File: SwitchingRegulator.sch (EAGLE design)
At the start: 31 parts, among them J1 APP_2POS_CONFIG5V_HORIZ, J2 APP_2POS_CONFIG5V_HORIZ, J3 APP_2POS_CONFIG5V_HORIZ, Q1 Q_OKI-78SR, Q2 Q_CSD18532KCSPCB

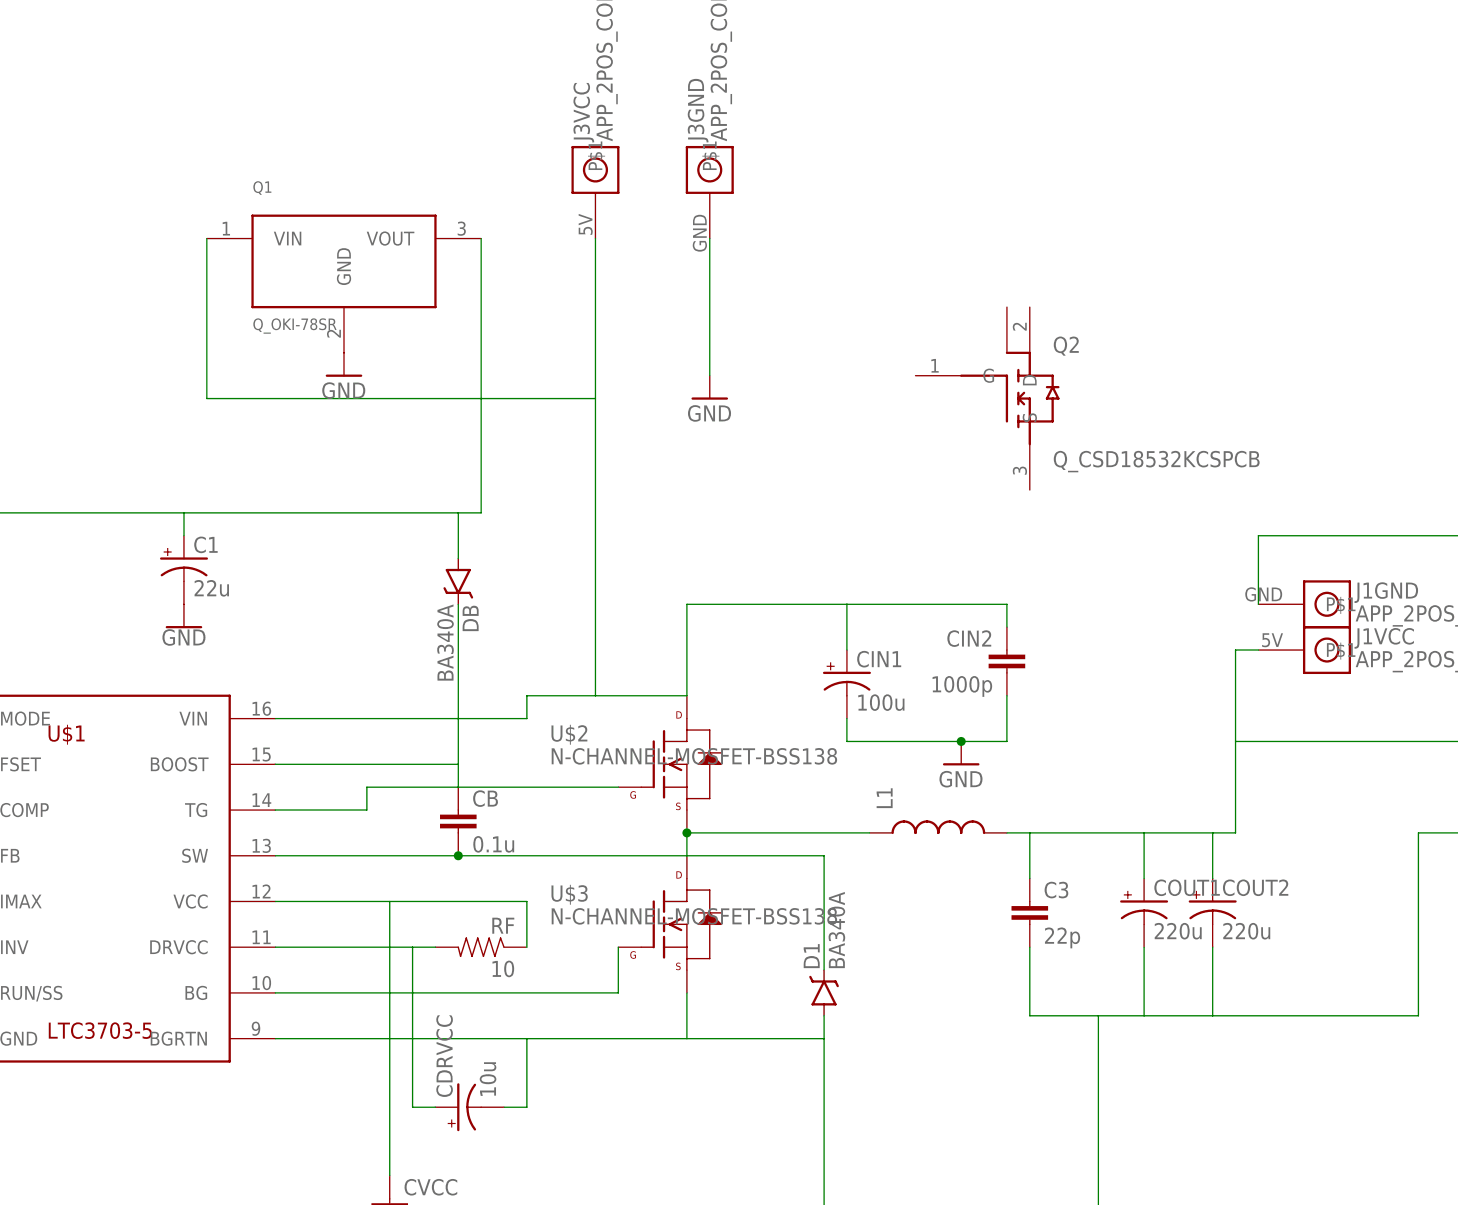
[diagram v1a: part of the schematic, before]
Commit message: Updated with all real components
Added devices for inductor, diodes, and mosfets
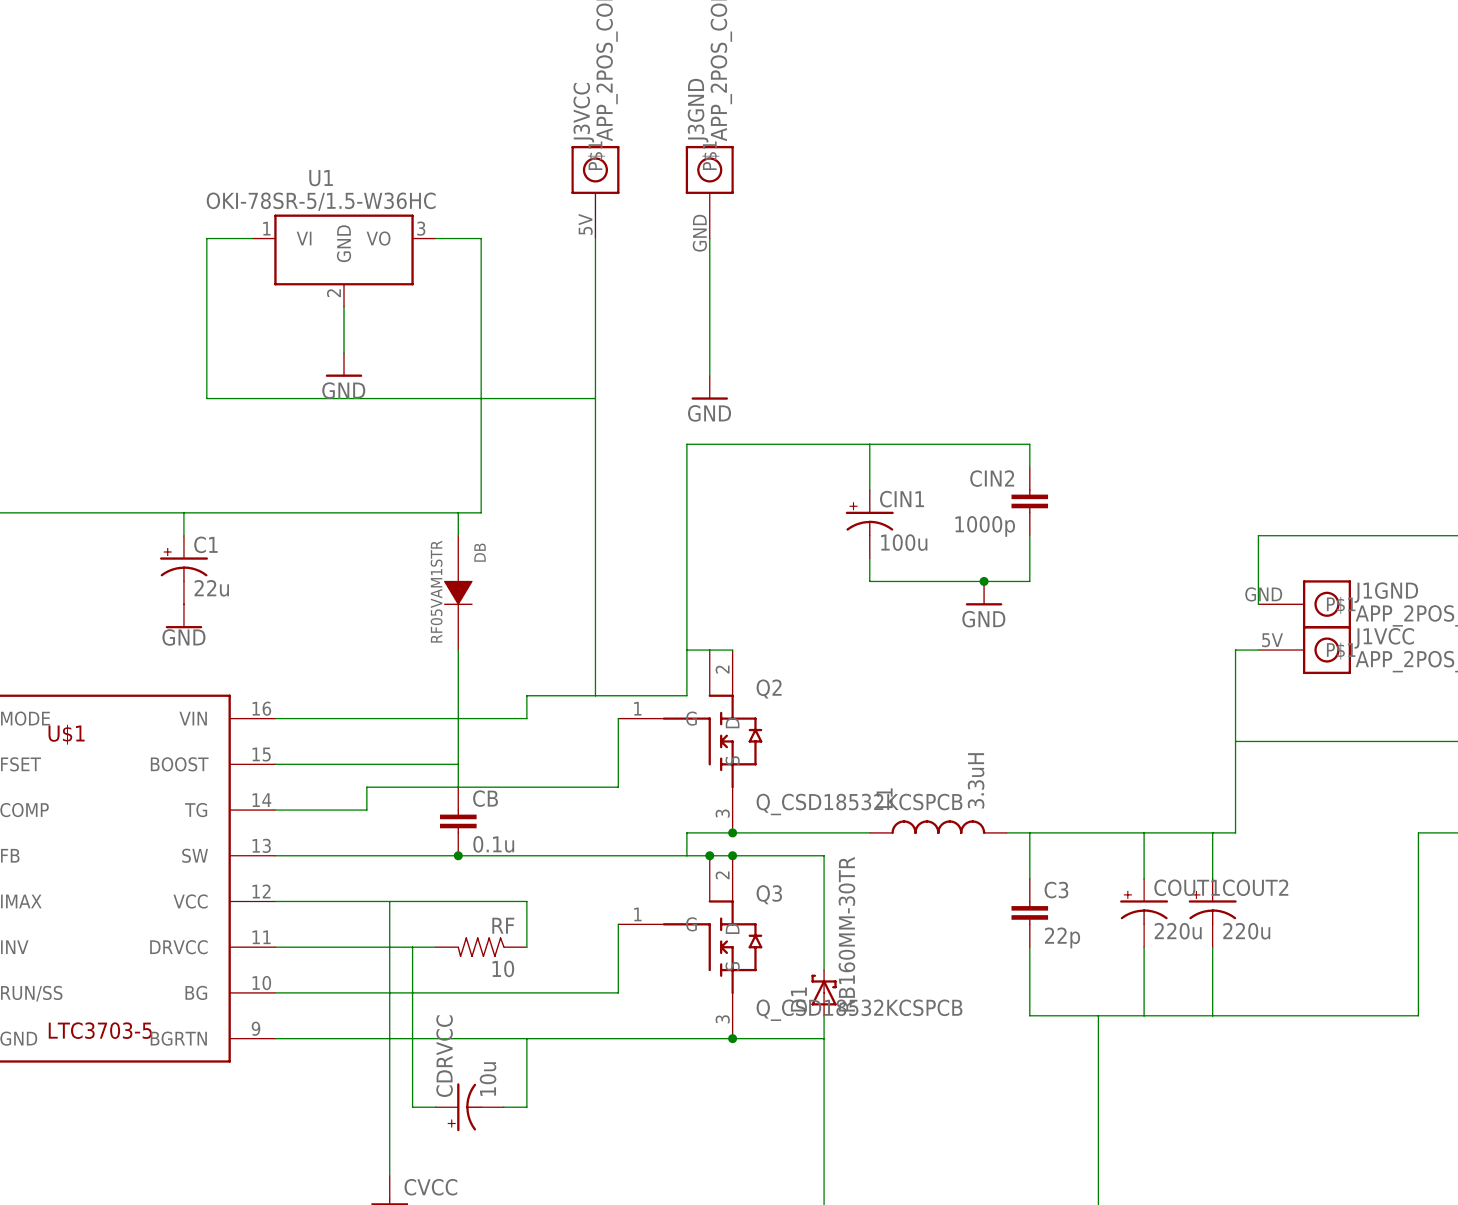
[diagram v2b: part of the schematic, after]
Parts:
- removed Q1: Q_OKI-78SR, MRDT-2014-All:Q_OKI-78SR
- removed U$2, U$3: N-CHANNEL-MOSFET-BSS138, GeekAmmo:N-CHANNEL-MOSFET-BSS138
- added Q3: Q_CSD18532KCSPCB, MRDT-2014-All:Q_CSD18532KCSPCB
- added U1: OKI-78SR-5/1.5-W36HC, MRDT-ICs:OKI-78SR-5/1.5-W36HC
- CIN1: device MRDT-2015-PowerBoard:B41858C9107M000 -> buckconverter:B41858C9107M000
- COUT1, COUT2: device MRDT-2015-PowerBoard:EGPD101ELL221MK25H -> buckconverter:EGPD101ELL221MK25H
- D1: value BA340A -> RB160MM-30TR; device SparkFun-DiscreteSemi:B340A -> buckconverter:RB160MM-30TR
- DB: value BA340A -> RF05VAM1STR; device SparkFun-DiscreteSemi:B340A -> buckconverter:RF05VAM1STR
- L1: value (none) -> 3.3uH; device SparkFun-Passives:INDUCTOR0805 -> buckconverter:PQ3218-3R3-70-T
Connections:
- net GND: now also Q3.S, U1.GND; no longer Q1.GND, U$3.S
- net N$1: now also DB.K; no longer DB.C
- net N$16: now also Q3.G; no longer U$3.G
- net N$17: now also Q2.S, Q3.D, Q3.P$1; no longer U$2.S, U$3.D
- net N$2: now also Q2.G; no longer U$2.G
- net N$5: now also U1.VO; no longer Q1.VOUT
- net VBATT: now also Q2.D, Q2.P$1, U1.VI; no longer Q1.VIN, U$2.D
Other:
- moved on the sheet: CIN1, CIN2, Q2

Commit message: Board design initiated
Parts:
- CDRVCC: device SparkFun-Passives:CAP_POL1206 -> SparkFun-Passives:CAP0603-CAP
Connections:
- net GND: now also CDRVCC.2; no longer CDRVCC.-
- net N$15: now also CDRVCC.1; no longer CDRVCC.+
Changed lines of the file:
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@@
 <?xml version="1.0" encoding="utf-8"?>
 <!DOCTYPE eagle SYSTEM "eagle.dtd">
-<eagle version="7.4.0">
+<eagle version="8.3.2">
 <drawing>
 <settings>
 <setting alwaysvectorfont="no"/>
+<setting keepoldvectorfont="yes"/>
 <setting verticaltext="up"/>
 </settings>
@@
 <part name="GND1" library="SparkFun-Aesthetics" deviceset="GND" device=""/>
 <part name="GND3" library="SparkFun-Aesthetics" deviceset="GND" device=""/>
-<part name="CDRVCC" library="SparkFun-Passives" deviceset="CAP_POL" device="1206" value="10u"/>
 <part name="GND4" library="SparkFun-Aesthetics" deviceset="GND" device=""/>
 <part name="GND5" library="SparkFun-Aesthetics" deviceset="GND" device=""/>
@@
 <part name="DB" library="buckconverter" deviceset="RF05VAM1STR" device=""/>
 <part name="U1" library="MRDT-ICs" deviceset="OKI-78SR-*/1.5-W36?C" device="H" technology="5"/>
+<part name="CDRVCC" library="SparkFun-Passives" deviceset="CAP" device="0603-CAP" value="10u"/>
 </parts>
 <sheets>
@@
 <instance part="GND1" gate="1" x="30.48" y="73.66"/>
 <instance part="GND3" gate="1" x="182.88" y="147.32"/>
-<instance part="CDRVCC" gate="G$1" x="124.46" y="91.44" rot="R90"/>
 <instance part="GND4" gate="1" x="152.4" y="170.18"/>
 <instance part="GND5" gate="1" x="111.76" y="172.72"/>
@@
 <instance part="DB" gate="G$1" x="124.46" y="147.32" rot="R270"/>
 <instance part="U1" gate="G$1" x="109.22" y="187.96"/>
+<instance part="CDRVCC" gate="G$1" x="127" y="91.44" rot="R90"/>
 </instances>
 <busses>
@@
 <wire x1="195.58" y1="101.6" x2="195.58" y2="76.2" width="0.1524" layer="91"/>
 <wire x1="195.58" y1="76.2" x2="165.1" y2="76.2" width="0.1524" layer="91"/>
-<pinref part="CDRVCC" gate="G$1" pin="-"/>
 <wire x1="129.54" y1="91.44" x2="132.08" y2="91.44" width="0.1524" layer="91"/>
 <wire x1="132.08" y1="91.44" x2="132.08" y2="99.06" width="0.1524" layer="91"/>
@@
 <junction x="154.94" y="99.06"/>
 <pinref part="D1" gate="G$1" pin="A"/>
+<pinref part="CDRVCC" gate="G$1" pin="2"/>
 </segment>
 <segment>
@@
 <pinref part="U$1" gate="G$1" pin="DRVCC"/>
 <wire x1="121.92" y1="109.22" x2="119.38" y2="109.22" width="0.1524" layer="91"/>
-<pinref part="CDRVCC" gate="G$1" pin="+"/>
 <wire x1="119.38" y1="109.22" x2="104.14" y2="109.22" width="0.1524" layer="91"/>
 <wire x1="121.92" y1="91.44" x2="119.38" y2="91.44" width="0.1524" layer="91"/>
 <wire x1="119.38" y1="91.44" x2="119.38" y2="109.22" width="0.1524" layer="91"/>
-</segment>
-</net>
+<pinref part="CDRVCC" gate="G$1" pin="1"/>
+</segment>
+</net>

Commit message: Major rearrangements
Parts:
- D1: value RB160MM-30TR -> RBR3MM30ATR; device buckconverter:RB160MM-30TR -> buckconverter:RBR3MM30ATR
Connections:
- removed net N$12: CC3.2, R1.1
- removed net N$5: C1.+, DB.A, U$1.MODE, U1.VO
- net N$15: now also C1.+, DB.A, U$1.MODE, U1.VO
- net VOUT12+: now also CC3.2, R1.1
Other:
- moved on the sheet: CB
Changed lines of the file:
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@@
 <part name="CIN1" library="buckconverter" deviceset="B41858C9107M000" device="" value="100u"/>
 <part name="Q3" library="MRDT-2014-All" deviceset="Q_CSD18532KCS" device="PCB"/>
-<part name="D1" library="buckconverter" deviceset="RB160MM-30TR" device=""/>
+<part name="D1" library="buckconverter" deviceset="RBR3MM30ATR" device=""/>
 <part name="DB" library="buckconverter" deviceset="RF05VAM1STR" device=""/>
 <part name="U1" library="MRDT-ICs" deviceset="OKI-78SR-*/1.5-W36?C" device="H" technology="5"/>
@@
 </plain>
 <instances>
-<instance part="CB" gate="G$1" x="124.46" y="121.92"/>
+<instance part="CB" gate="G$1" x="144.78" y="121.92"/>
 <instance part="CVCC" gate="G$1" x="116.84" y="78.74"/>
 <instance part="CC3" gate="G$1" x="-30.48" y="76.2"/>
@@
 <wire x1="0" y1="109.22" x2="0" y2="116.84" width="0.1524" layer="91"/>
 <wire x1="12.7" y1="109.22" x2="0" y2="109.22" width="0.1524" layer="91"/>
+<junction x="0" y="109.22"/>
+<junction x="-10.16" y="96.52"/>
+<junction x="0" y="116.84"/>
+<junction x="38.1" y="116.84"/>
 </segment>
 </net>
@@
 <pinref part="D1" gate="G$1" pin="A"/>
 <pinref part="CDRVCC" gate="G$1" pin="2"/>
+<junction x="30.48" y="114.3"/>
+<junction x="30.48" y="104.14"/>
+<junction x="30.48" y="99.06"/>
+<junction x="45.72" y="99.06"/>
+<junction x="132.08" y="99.06"/>
+<junction x="165.1" y="76.2"/>
+<junction x="195.58" y="101.6"/>
+<junction x="200.66" y="101.6"/>
+<junction x="208.28" y="101.6"/>
+<junction x="243.84" y="137.16"/>
+<junction x="30.48" y="109.22"/>
+<junction x="116.84" y="76.2"/>
+<junction x="165.1" y="99.06"/>
 </segment>
 <segment>
@@
 </segment>
 </net>
-<net name="N$12" class="0">
-<segment>
-<pinref part="CC3" gate="G$1" pin="2"/>
-<wire x1="-30.48" y1="73.66" x2="-30.48" y2="66.04" width="0.1524" layer="91"/>
-<pinref part="R1" gate="G$1" pin="1"/>
-<wire x1="-30.48" y1="66.04" x2="-10.16" y2="66.04" width="0.1524" layer="91"/>
-<wire x1="-10.16" y1="66.04" x2="-10.16" y2="86.36" width="0.1524" layer="91"/>
-</segment>
-</net>
 <net name="N$13" class="0">
 <segment>
@@
 <wire x1="132.08" y1="109.22" x2="132.08" y2="114.3" width="0.1524" layer="91"/>
 <wire x1="132.08" y1="114.3" x2="116.84" y2="114.3" width="0.1524" layer="91"/>
+<junction x="116.84" y="114.3"/>
 </segment>
 </net>
@@
 <wire x1="119.38" y1="91.44" x2="119.38" y2="109.22" width="0.1524" layer="91"/>
 <pinref part="CDRVCC" gate="G$1" pin="1"/>
+<pinref part="U$1" gate="G$1" pin="MODE"/>
+<wire x1="66.04" y1="134.62" x2="58.42" y2="134.62" width="0.1524" layer="91"/>
+<wire x1="58.42" y1="134.62" x2="58.42" y2="157.48" width="0.1524" layer="91"/>
+<wire x1="58.42" y1="157.48" x2="93.98" y2="157.48" width="0.1524" layer="91"/>
+<wire x1="93.98" y1="157.48" x2="119.38" y2="157.48" width="0.1524" layer="91"/>
+<wire x1="119.38" y1="157.48" x2="124.46" y2="157.48" width="0.1524" layer="91"/>
+<wire x1="124.46" y1="157.48" x2="127" y2="157.48" width="0.1524" layer="91"/>
+<wire x1="127" y1="187.96" x2="127" y2="157.48" width="0.1524" layer="91"/>
+<pinref part="C1" gate="G$1" pin="+"/>
+<wire x1="93.98" y1="157.48" x2="93.98" y2="154.94" width="0.1524" layer="91"/>
+<pinref part="DB" gate="G$1" pin="A"/>
+<wire x1="124.46" y1="154.94" x2="124.46" y2="157.48" width="0.1524" layer="91"/>
+<pinref part="U1" gate="G$1" pin="VO"/>
+<wire x1="121.92" y1="187.96" x2="127" y2="187.96" width="0.1524" layer="91"/>
+<wire x1="119.38" y1="109.22" x2="119.38" y2="157.48" width="0.1524" layer="91"/>
+<junction x="119.38" y="109.22"/>
+<junction x="124.46" y="157.48"/>
+<junction x="119.38" y="157.48"/>
+<junction x="93.98" y="157.48"/>
 </segment>
 </net>
@@
 <segment>
 <pinref part="U$1" gate="G$1" pin="SW"/>
-<wire x1="149.86" y1="119.38" x2="124.46" y2="119.38" width="0.1524" layer="91"/>
-<wire x1="124.46" y1="119.38" x2="104.14" y2="119.38" width="0.1524" layer="91"/>
+<wire x1="149.86" y1="119.38" x2="144.78" y2="119.38" width="0.1524" layer="91"/>
+<wire x1="144.78" y1="119.38" x2="104.14" y2="119.38" width="0.1524" layer="91"/>
 <wire x1="165.1" y1="106.68" x2="165.1" y2="119.38" width="0.1524" layer="91"/>
 <wire x1="165.1" y1="119.38" x2="154.94" y2="119.38" width="0.1524" layer="91"/>
@@
 <wire x1="149.86" y1="121.92" x2="149.86" y2="119.38" width="0.1524" layer="91"/>
 <pinref part="CB" gate="G$1" pin="2"/>
-<junction x="124.46" y="119.38"/>
+<junction x="144.78" y="119.38"/>
 <pinref part="L1" gate="G$1" pin="1"/>
 <pinref part="Q2" gate="G$1" pin="S"/>
@@
 <junction x="152.4" y="119.38"/>
 <pinref part="D1" gate="G$1" pin="C"/>
+<junction x="149.86" y="119.38"/>
 </segment>
 </net>
@@
 <segment>
 <pinref part="U$1" gate="G$1" pin="BOOST"/>
-<pinref part="CB" gate="G$1" pin="1"/>
 <wire x1="104.14" y1="129.54" x2="124.46" y2="129.54" width="0.1524" layer="91"/>
-<wire x1="124.46" y1="129.54" x2="124.46" y2="127" width="0.1524" layer="91"/>
 <pinref part="DB" gate="G$1" pin="K"/>
 <wire x1="124.46" y1="142.24" x2="124.46" y2="129.54" width="0.1524" layer="91"/>
+<pinref part="CB" gate="G$1" pin="1"/>
+<wire x1="124.46" y1="129.54" x2="144.78" y2="129.54" width="0.1524" layer="91"/>
+<wire x1="144.78" y1="129.54" x2="144.78" y2="127" width="0.1524" layer="91"/>
+<junction x="124.46" y="129.54"/>
 </segment>
 </net>
@@
 <pinref part="Q2" gate="G$1" pin="G"/>
 <wire x1="142.24" y1="134.62" x2="142.24" y2="127" width="0.1524" layer="91"/>
-</segment>
-</net>
-<net name="N$5" class="0">
-<segment>
-<pinref part="U$1" gate="G$1" pin="MODE"/>
-<wire x1="66.04" y1="134.62" x2="58.42" y2="134.62" width="0.1524" layer="91"/>
-<wire x1="58.42" y1="134.62" x2="58.42" y2="157.48" width="0.1524" layer="91"/>
-<wire x1="58.42" y1="157.48" x2="93.98" y2="157.48" width="0.1524" layer="91"/>
-<wire x1="93.98" y1="157.48" x2="124.46" y2="157.48" width="0.1524" layer="91"/>
-<wire x1="124.46" y1="157.48" x2="127" y2="157.48" width="0.1524" layer="91"/>
-<wire x1="127" y1="187.96" x2="127" y2="157.48" width="0.1524" layer="91"/>
-<pinref part="C1" gate="G$1" pin="+"/>
-<wire x1="93.98" y1="157.48" x2="93.98" y2="154.94" width="0.1524" layer="91"/>
-<pinref part="DB" gate="G$1" pin="A"/>
-<wire x1="124.46" y1="154.94" x2="124.46" y2="157.48" width="0.1524" layer="91"/>
-<pinref part="U1" gate="G$1" pin="VO"/>
-<wire x1="121.92" y1="187.96" x2="127" y2="187.96" width="0.1524" layer="91"/>
 </segment>
 </net>
@@
 <pinref part="U1" gate="G$1" pin="VI"/>
 <wire x1="101.6" y1="187.96" x2="96.52" y2="187.96" width="0.1524" layer="91"/>
+<junction x="139.7" y="137.16"/>
+<junction x="149.86" y="142.24"/>
+<junction x="152.4" y="142.24"/>
+<junction x="170.18" y="165.1"/>
+<junction x="139.7" y="170.18"/>
 </segment>
 </net>
@@
 <pinref part="COUT1" gate="G$1" pin="+"/>
 <pinref part="COUT2" gate="G$1" pin="+"/>
-</segment>
-</net>
+<pinref part="CC3" gate="G$1" pin="2"/>
+<wire x1="-30.48" y1="73.66" x2="-30.48" y2="66.04" width="0.1524" layer="91"/>
+<pinref part="R1" gate="G$1" pin="1"/>
+<wire x1="-30.48" y1="66.04" x2="-10.16" y2="66.04" width="0.1524" layer="91"/>
+<wire x1="-10.16" y1="66.04" x2="-10.16" y2="68.58" width="0.1524" layer="91"/>
+<wire x1="-10.16" y1="68.58" x2="-10.16" y2="86.36" width="0.1524" layer="91"/>
+<wire x1="-10.16" y1="68.58" x2="210.82" y2="68.58" width="0.1524" layer="91"/>
+<wire x1="210.82" y1="68.58" x2="210.82" y2="121.92" width="0.1524" layer="91"/>
+<junction x="-10.16" y="68.58"/>
+<junction x="200.66" y="121.92"/>
+<junction x="187.96" y="121.92"/>
+<junction x="208.28" y="121.92"/>
+<junction x="210.82" y="121.92"/>
+<junction x="210.82" y="132.08"/>
+</segment>
+</net>

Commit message: New layout, do power power path
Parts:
- removed J3: APP_2POS_CONFIG5V_HORIZ, MRDT-Connectors:APP_2POS_CONFIG5V_HORIZ
- added J4: APP_2POS_CONFIG12V_HORIZ, MRDT-Connectors:APP_2POS_CONFIG12V_HORIZ
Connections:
- net GND: now also J4GND.P$1; no longer J3GND.P$1
- net VBATT: now also J4VCC.P$1; no longer J3VCC.P$1
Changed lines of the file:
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@@
 <?xml version="1.0" encoding="utf-8"?>
 <!DOCTYPE eagle SYSTEM "eagle.dtd">
-<eagle version="7.4.0">
+<eagle version="8.4.0">
 <drawing>
 <settings>
 <setting alwaysvectorfont="no"/>
+<setting keepoldvectorfont="yes"/>
 <setting verticaltext="up"/>
 </settings>
@@
 <class number="0" name="default" width="0" drill="0">
 </class>
+<class number="1" name="high_current" width="9.525" drill="0">
+</class>
+<class number="2" name="fet_drive" width="0.508" drill="0">
+<clearance class="2" value="0.0762"/>
+</class>
+<class number="3" name="sample" width="0.127" drill="0">
+<clearance class="3" value="0.0762"/>
+</class>
 </classes>
 <parts>
@@
 <part name="J1" library="MRDT-Connectors" deviceset="APP_2POS_CONFIG" device="5V_HORIZ"/>
 <part name="J2" library="MRDT-Connectors" deviceset="APP_2POS_CONFIG" device="5V_HORIZ"/>
-<part name="J3" library="MRDT-Connectors" deviceset="APP_2POS_CONFIG" device="5V_HORIZ"/>
 <part name="Q2" library="MRDT-2014-All" deviceset="Q_CSD18532KCS" device="PCB"/>
 <part name="C1" library="buckconverter" deviceset="UCZ1K220MCL1GS" device="" value="22u"/>
@@
 <part name="U1" library="MRDT-ICs" deviceset="OKI-78SR-*/1.5-W36?C" device="H" technology="5"/>
 <part name="CDRVCC" library="SparkFun-Passives" deviceset="CAP" device="0603-CAP" value="10u"/>
+<part name="J4" library="MRDT-Connectors" deviceset="APP_2POS_CONFIG" device="12V_HORIZ"/>
 </parts>
 <sheets>
@@
 <instance part="J2" gate="GND" x="256.54" y="137.16"/>
 <instance part="J2" gate="VCC" x="256.54" y="132.08"/>
-<instance part="J3" gate="GND" x="152.4" y="195.58" rot="R90"/>
-<instance part="J3" gate="VCC" x="139.7" y="195.58" rot="R90"/>
 <instance part="Q2" gate="G$1" x="154.94" y="132.08"/>
 <instance part="C1" gate="G$1" x="93.98" y="149.86"/>
@@
 <instance part="U1" gate="G$1" x="109.22" y="187.96"/>
 <instance part="CDRVCC" gate="G$1" x="127" y="91.44" rot="R90"/>
+<instance part="J4" gate="GND" x="152.4" y="195.58" rot="R90"/>
+<instance part="J4" gate="VCC" x="139.7" y="195.58" rot="R90"/>
 </instances>
 <busses>
@@
 <segment>
 <pinref part="GND4" gate="1" pin="GND"/>
-<pinref part="J3" gate="GND" pin="P$1"/>
 <wire x1="152.4" y1="172.72" x2="152.4" y2="187.96" width="0.1524" layer="91"/>
+<pinref part="J4" gate="GND" pin="P$1"/>
 </segment>
 <segment>
@@
 </segment>
 </net>
-<net name="N$16" class="0">
+<net name="N$16" class="2">
 <segment>
 <pinref part="U$1" gate="G$1" pin="BG"/>
@@
 </segment>
 </net>
-<net name="N$2" class="0">
+<net name="N$2" class="2">
 <segment>
 <pinref part="U$1" gate="G$1" pin="TG"/>
@@
 <wire x1="96.52" y1="187.96" x2="96.52" y2="170.18" width="0.1524" layer="91"/>
 <wire x1="96.52" y1="170.18" x2="139.7" y2="170.18" width="0.1524" layer="91"/>
-<pinref part="J3" gate="VCC" pin="P$1"/>
 <wire x1="139.7" y1="187.96" x2="139.7" y2="170.18" width="0.1524" layer="91"/>
 <pinref part="CIN2" gate="G$1" pin="1"/>
@@
 <junction x="170.18" y="165.1"/>
 <junction x="139.7" y="170.18"/>
-</segment>
-</net>
+<pinref part="J4" gate="VCC" pin="P$1"/>
+</segment>
+</net>
